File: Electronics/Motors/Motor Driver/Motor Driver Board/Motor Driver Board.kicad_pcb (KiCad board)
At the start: 2 copper layers, 136 parts, among them IC1 STM32H723ZGT6, IC2 TJA1057GT/3, IC3 ESDA6V1W5, IC4 ESDA6V1W5, IC5 TPS54295PWPR, J1 TYPE-C-31-M-12, J2 Screw_Terminal_01x02, J3 TC2030, J4 XT60PW-F, J5 XT60PW-F, J6 XT60PW-F, J7 XT60PW-M, J8 Screw_Terminal_01x02, SW1 SW_DIP_x02, T1 NVMFS4C05NT1G, T10 NVMFS4C05NT1G, T11 NVMFS4C05NT1G, T12 NVMFS4C05NT1G, T2 NVMFS4C05NT1G, T3 NVMFS4C05NT1G, T4 NVMFS4C05NT1G, T5 NVMFS4C05NT1G, T6 NVMFS4C05NT1G, T7 NVMFS4C05NT1G, T8 NVMFS4C05NT1G, T9 NVMFS4C05NT1G, U1 LSM6DS3, U2 DRV8701ERGER, U3 DRV8701ERGER, U4 DRV8701ERGER, X1 25MHz_Clock, X2 32.768kHz_Clock

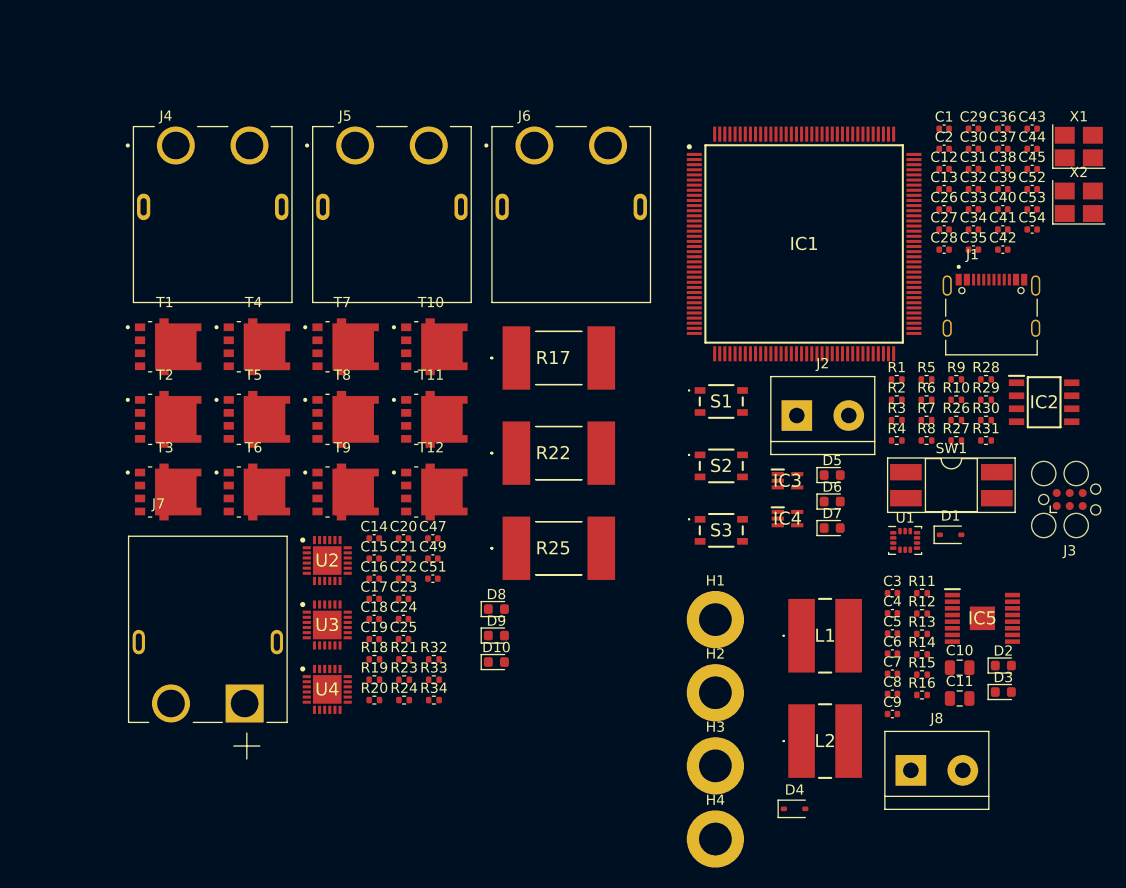
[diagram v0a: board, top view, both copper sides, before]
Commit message: Schematic updates
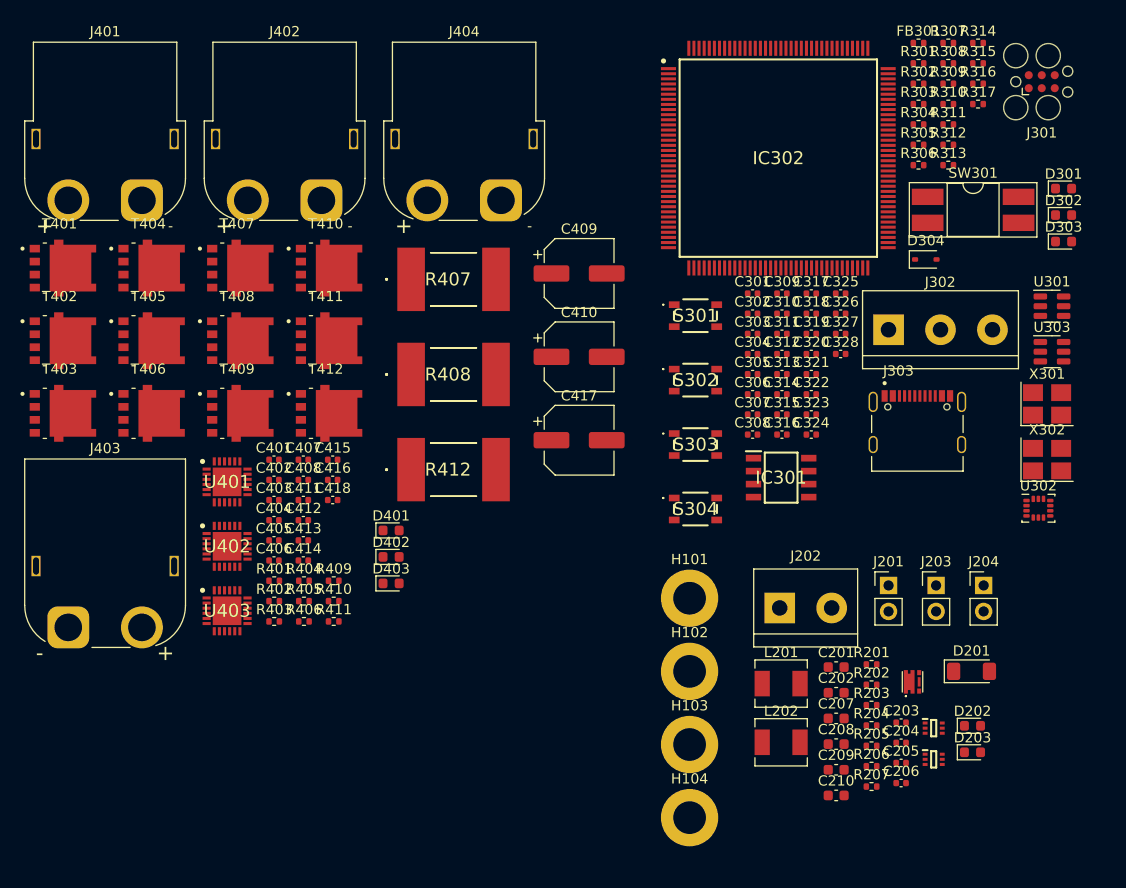
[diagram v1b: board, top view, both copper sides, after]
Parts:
- removed C1, C12, C13, C15, C2, C20, C24, C28, C30, C32, C33, C34, C35, C36, C37, C39, C40, C41, C42, C43, C44, C47, C49, C51, C7, C8: 100n, Capacitor_SMD:C_0402_1005Metric
- removed C10, C11: 47u, Capacitor_SMD:C_0805_2012Metric
- removed C14, C16, C17, C18, C19, C21, C22, C23, C25, C29, C31, C9: 1u, Capacitor_SMD:C_0402_1005Metric
- removed C26, C27: 2u2, Capacitor_SMD:C_0402_1005Metric
- removed C3, C38, C4, C45: 10u, Capacitor_SMD:C_0402_1005Metric
- removed C5, C52, C53, C54, C6: 10n, Capacitor_SMD:C_0402_1005Metric
- removed D1, D4: BAT760-115, Diode_SMD:D_SOD-323
- removed D10, D5, D8, D9: Red, LED_SMD:LED_0603_1608Metric
- removed D2, D3: LED_R, LED_SMD:LED_0603_1608Metric
- removed D6: Green, LED_SMD:LED_0603_1608Metric
- removed D7: Blue, LED_SMD:LED_0603_1608Metric
- removed H1, H2, H3, H4: MountingHole_Pad, MountingHole:MountingHole_3.2mm_M3_DIN965_Pad
- removed IC1: STM32H723ZGT6, MSL Footprints:QFP50P2200X2200X160-144N
- removed IC2: TJA1057GT/3, MSL Footprints:SOIC127P600X175-8N
- removed IC3, IC4: ESDA6V1W5, footprints:SOT65P210X110-5N
- removed IC5: TPS54295PWPR, MSL Footprints:SOP65P640X120-17N
- removed J1: TYPE-C-31-M-12, MSL Footprints:HRO_TYPE-C-31-M-12
- removed J2, J8: Screw_Terminal_01x02, TerminalBlock:TerminalBlock_bornier-2_P5.08mm
- removed J3: TC2030, Connector:Tag-Connect_TC2030-IDC-FP_2x03_P1.27mm_Vertical
- removed J4, J5, J6: XT60PW-F, MSL Footprints:AMASS_XT60PW-F
- removed J7: XT60PW-M, MSL Footprints:AMASS_XT60PW-M
- removed L1: 3u3, MSL Footprints:29332C
- removed L2: 2u2, MSL Footprints:29222C
- removed R1, R15, R2, R3, R4, R5, R6: 2k2, Resistor_SMD:R_0402_1005Metric
- removed R10, R14, R18, R19, R20, R21, R23, R24, R26, R27, R28: 10k, Resistor_SMD:R_0402_1005Metric
- removed R11: 124k, Resistor_SMD:R_0402_1005Metric
- removed R12: 22k1, Resistor_SMD:R_0402_1005Metric
- removed R13: 33k, Resistor_SMD:R_0402_1005Metric
- removed R16, R29, R30, R31, R32, R33, R34: 1k5, Resistor_SMD:R_0402_1005Metric
- removed R17, R22, R25: CSS2H-3920K-5L00F, MSL Footprints:CSS2H3920K5L00F
- removed R7, R8: 5k1, Resistor_SMD:R_0402_1005Metric
- removed R9: 120R, Resistor_SMD:R_0402_1005Metric
- removed S1, S2, S3: TS20-42-25-WT-160-SMT-TR, MSL Footprints:TS204225WT160SMTTRMSL
- removed SW1: SW_DIP_x02, Package_DIP:DIP-4_W8.89mm_SMDSocket_LongPads
- removed T1, T10, T11, T12, T2, T3, T4, T5, T6, T7, T8, T9: NVMFS4C05NT1G, MSL Footprints:TRANS_NVMFS5834NLWFT1G
- removed U1: LSM6DS3, Package_LGA:LGA-14_3x2.5mm_P0.5mm_LayoutBorder3x4y
- removed U2, U3, U4: DRV8701ERGER, MSL Footprints:QFN50P400X400X100-25N-D
- removed X1: 25MHz_Clock, Oscillator:Oscillator_SMD_Abracon_ASE-4Pin_3.2x2.5mm_HandSoldering
- removed X2: 32.768kHz_Clock, Oscillator:Oscillator_SMD_Abracon_ASE-4Pin_3.2x2.5mm_HandSoldering
- added C201: 22u, Capacitor_SMD:C_0603_1608Metric, F.Cu at (172.6, 109.8)
- added C202: 22u, Capacitor_SMD:C_0603_1608Metric, F.Cu at (172.6, 112.3)
- added C203: 100n, Capacitor_SMD:C_0402_1005Metric, F.Cu at (178.9, 115.2)
- added C204: 100n, Capacitor_SMD:C_0402_1005Metric, F.Cu at (178.9, 117.2)
- added C205: 100n, Capacitor_SMD:C_0402_1005Metric, F.Cu at (178.9, 119.2)
- added C206: 100n, Capacitor_SMD:C_0402_1005Metric, F.Cu at (178.9, 121.1)
- added C207: 22u, Capacitor_SMD:C_0603_1608Metric, F.Cu at (172.6, 114.8)
- added C208: 22u, Capacitor_SMD:C_0603_1608Metric, F.Cu at (172.6, 117.3)
- added C209: 22u, Capacitor_SMD:C_0603_1608Metric, F.Cu at (172.6, 119.8)
- added C210: 22u, Capacitor_SMD:C_0603_1608Metric, F.Cu at (172.6, 122.3)
- added C301: 100n, Capacitor_SMD:C_0402_1005Metric, F.Cu at (164.4, 73.3)
- added C302: 100n, Capacitor_SMD:C_0402_1005Metric, F.Cu at (164.4, 75.2)
- added C303: 10n, Capacitor_SMD:C_0402_1005Metric, F.Cu at (164.4, 77.2)
- added C304: 10n, Capacitor_SMD:C_0402_1005Metric, F.Cu at (164.4, 79.2)
- added C305: 10n, Capacitor_SMD:C_0402_1005Metric, F.Cu at (164.4, 81.1)
- added C306: 100n, Capacitor_SMD:C_0402_1005Metric, F.Cu at (164.4, 83.1)
- added C307: 1u, Capacitor_SMD:C_0402_1005Metric, F.Cu at (164.4, 85.1)
- added C308: 100n, Capacitor_SMD:C_0402_1005Metric, F.Cu at (164.4, 87.0)
- added C309: 100n, Capacitor_SMD:C_0402_1005Metric, F.Cu at (167.3, 73.3)
- added C310: 100n, Capacitor_SMD:C_0402_1005Metric, F.Cu at (167.3, 75.2)
- added C311: 1u, Capacitor_SMD:C_0402_1005Metric, F.Cu at (167.3, 77.2)
- added C312: 100n, Capacitor_SMD:C_0402_1005Metric, F.Cu at (167.3, 79.2)
- added C313: 100n, Capacitor_SMD:C_0402_1005Metric, F.Cu at (167.3, 81.1)
- added C314: 100n, Capacitor_SMD:C_0402_1005Metric, F.Cu at (167.3, 83.1)
- added C315: 100n, Capacitor_SMD:C_0402_1005Metric, F.Cu at (167.3, 85.1)
- added C316: 10u, Capacitor_SMD:C_0402_1005Metric, F.Cu at (167.3, 87.0)
- added C317: 100n, Capacitor_SMD:C_0402_1005Metric, F.Cu at (170.1, 73.3)
- added C318: 100n, Capacitor_SMD:C_0402_1005Metric, F.Cu at (170.1, 75.2)
- added C319: 100n, Capacitor_SMD:C_0402_1005Metric, F.Cu at (170.1, 77.2)
- added C320: 100n, Capacitor_SMD:C_0402_1005Metric, F.Cu at (170.1, 79.2)
- added C321: 2u2, Capacitor_SMD:C_0402_1005Metric, F.Cu at (170.1, 81.1)
- added C322: 100n, Capacitor_SMD:C_0402_1005Metric, F.Cu at (170.1, 83.1)
- added C323: 100n, Capacitor_SMD:C_0402_1005Metric, F.Cu at (170.1, 85.1)
- added C324: 10u, Capacitor_SMD:C_0402_1005Metric, F.Cu at (170.1, 87.0)
- added C325: 2u2, Capacitor_SMD:C_0402_1005Metric, F.Cu at (173.0, 73.3)
- added C326: 100n, Capacitor_SMD:C_0402_1005Metric, F.Cu at (173.0, 75.2)
- added C327: 100n, Capacitor_SMD:C_0402_1005Metric, F.Cu at (173.0, 77.2)
- added C328: 10n, Capacitor_SMD:C_0402_1005Metric, F.Cu at (173.0, 79.2)
- added C401: 1u, Capacitor_SMD:C_0402_1005Metric, F.Cu at (117.6, 89.5)
- added C402: 1u, Capacitor_SMD:C_0402_1005Metric, F.Cu at (117.6, 91.5)
- added C403: 1u, Capacitor_SMD:C_0402_1005Metric, F.Cu at (117.6, 93.5)
- added C404: 1u, Capacitor_SMD:C_0402_1005Metric, F.Cu at (117.6, 95.4)
- added C405: 100n, Capacitor_SMD:C_0402_1005Metric, F.Cu at (117.6, 97.4)
- added C406: 100n, Capacitor_SMD:C_0402_1005Metric, F.Cu at (117.6, 99.4)
- added C407: 1u, Capacitor_SMD:C_0402_1005Metric, F.Cu at (120.5, 89.5)
- added C408: 1u, Capacitor_SMD:C_0402_1005Metric, F.Cu at (120.5, 91.5)
- added C409: 100u, Capacitor_SMD:CP_Elec_6.3x7.7, F.Cu at (147.4, 71.3)
- added C410: 100u, Capacitor_SMD:CP_Elec_6.3x7.7, F.Cu at (147.4, 79.5)
- added C411: 100n, Capacitor_SMD:C_0402_1005Metric, F.Cu at (120.5, 93.5)
- added C412: 100n, Capacitor_SMD:C_0402_1005Metric, F.Cu at (120.5, 95.4)
- added C413: 1u, Capacitor_SMD:C_0402_1005Metric, F.Cu at (120.5, 97.4)
- added C414: 1u, Capacitor_SMD:C_0402_1005Metric, F.Cu at (120.5, 99.4)
- added C415: 100n, Capacitor_SMD:C_0402_1005Metric, F.Cu at (123.3, 89.5)
- added C416: 1u, Capacitor_SMD:C_0402_1005Metric, F.Cu at (123.3, 91.5)
- added C417: 100u, Capacitor_SMD:CP_Elec_6.3x7.7, F.Cu at (147.4, 87.6)
- added C418: 100n, Capacitor_SMD:C_0402_1005Metric, F.Cu at (123.3, 93.5)
- added D201: ZMM10V, Diode_SMD:D_MiniMELF, F.Cu at (185.8, 110.2)
- added D202: GREEN, LED_SMD:LED_0603_1608Metric, F.Cu at (185.9, 115.5)
- added D203: GREEN, LED_SMD:LED_0603_1608Metric, F.Cu at (185.9, 118.1)
- added D301: Red, LED_SMD:LED_0603_1608Metric, F.Cu at (194.8, 63.0)
- added D302: Green, LED_SMD:LED_0603_1608Metric, F.Cu at (194.8, 65.6)
- added D303: Blue, LED_SMD:LED_0603_1608Metric, F.Cu at (194.8, 68.2)
- added D304: BAT760-115, Diode_SMD:D_SOD-323, F.Cu at (181.3, 69.9)
- added D401: Red, LED_SMD:LED_0603_1608Metric, F.Cu at (129.1, 96.4)
- added D402: Red, LED_SMD:LED_0603_1608Metric, F.Cu at (129.1, 99.0)
- added D403: Red, LED_SMD:LED_0603_1608Metric, F.Cu at (129.1, 101.6)
- added FB301: 120R@100MHz, Resistor_SMD:R_0402_1005Metric, F.Cu at (180.6, 48.8)
- added H101: MountingHole_Pad, MountingHole:MountingHole_3.2mm_M3_DIN965_Pad, F.Cu at (158.2, 103.0)
- added H102: MountingHole_Pad, MountingHole:MountingHole_3.2mm_M3_DIN965_Pad, F.Cu at (158.2, 110.2)
- added H103: MountingHole_Pad, MountingHole:MountingHole_3.2mm_M3_DIN965_Pad, F.Cu at (158.2, 117.3)
- added H104: MountingHole_Pad, MountingHole:MountingHole_3.2mm_M3_DIN965_Pad, F.Cu at (158.2, 124.5)
- added IC201: TPS563202DRLR, MSL Footprints:SOTFL50P160X60-6N, F.Cu at (182.1, 115.8)
- added IC202: TPS563202DRLR, MSL Footprints:SOTFL50P160X60-6N, F.Cu at (182.1, 118.8)
- added IC301: TJA1057GT/3, MSL Footprints:SOIC127P600X175-8N, F.Cu at (167.2, 91.3)
- added IC302: STM32H723ZGT6, MSL Footprints:QFP50P2200X2200X160-144N, F.Cu at (166.9, 60.0)
- added J201: Conn_01x02_Pin, Connector_PinHeader_2.54mm:PinHeader_1x02_P2.54mm_Vertical, F.Cu at (177.7, 101.8)
- added J202: Screw_Terminal_01x02, TerminalBlock:TerminalBlock_bornier-2_P5.08mm, F.Cu at (167.0, 104.0)
- added J203: Conn_01x02_Pin, Connector_PinHeader_2.54mm:PinHeader_1x02_P2.54mm_Vertical, F.Cu at (182.3, 101.8)
- added J204: Conn_01x02_Pin, Connector_PinHeader_2.54mm:PinHeader_1x02_P2.54mm_Vertical, F.Cu at (187.0, 101.8)
- added J301: TC2030, Connector:Tag-Connect_TC2030-IDC-FP_2x03_P1.27mm_Vertical, F.Cu at (192.7, 52.5)
- added J302: Screw_Terminal_01x03, TerminalBlock:TerminalBlock_bornier-3_P5.08mm, F.Cu at (177.7, 76.8)
- added J303: TYPE-C-31-M-12, MSL Footprints:HRO_TYPE-C-31-M-12, F.Cu at (180.5, 88.0)
- added J401: XT60PW-F, Connector_AMASS:AMASS_XT60PW-F_1x02_P7.20mm_Horizontal, F.Cu at (104.7, 64.2)
- added J402: XT60PW-F, Connector_AMASS:AMASS_XT60PW-F_1x02_P7.20mm_Horizontal, F.Cu at (122.2, 64.2)
- added J403: XT60PW-M, Connector_AMASS:AMASS_XT60PW-M_1x02_P7.20mm_Horizontal, F.Cu at (97.5, 105.9)
- added J404: XT60PW-F, Connector_AMASS:AMASS_XT60PW-F_1x02_P7.20mm_Horizontal, F.Cu at (139.8, 64.2)
- added L201: 4u7, Inductor_SMD:L_Chilisin_BMRA00040420, F.Cu at (167.2, 111.4)
- added L202: 3u3, Inductor_SMD:L_Chilisin_BMRA00040420, F.Cu at (167.2, 117.1)
- added Q201: DMP3028LFDE, MSL Footprints:DMP2066UFDE7, F.Cu at (180.0, 111.2)
- added R201: 330R, Resistor_SMD:R_0402_1005Metric, F.Cu at (176.0, 109.5)
- added R202: 52k, Resistor_SMD:R_0402_1005Metric, F.Cu at (176.0, 111.5)
- added R203: 10k, Resistor_SMD:R_0402_1005Metric, F.Cu at (176.0, 113.5)
- added R204: 31k, Resistor_SMD:R_0402_1005Metric, F.Cu at (176.0, 115.5)
- added R205: 10k, Resistor_SMD:R_0402_1005Metric, F.Cu at (176.0, 117.5)
- added R206: 2k2, Resistor_SMD:R_0402_1005Metric, F.Cu at (176.0, 119.5)
- added R207: 1k5, Resistor_SMD:R_0402_1005Metric, F.Cu at (176.0, 121.5)
- added R301: 1k5, Resistor_SMD:R_0402_1005Metric, F.Cu at (180.6, 50.8)
- added R302: 1k5, Resistor_SMD:R_0402_1005Metric, F.Cu at (180.6, 52.8)
- added R303: 1k5, Resistor_SMD:R_0402_1005Metric, F.Cu at (180.6, 54.7)
- added R304: 10k, Resistor_SMD:R_0402_1005Metric, F.Cu at (180.6, 56.7)
- added R305: 10k, Resistor_SMD:R_0402_1005Metric, F.Cu at (180.6, 58.7)
- added R306: 10k, Resistor_SMD:R_0402_1005Metric, F.Cu at (180.6, 60.7)
- added R307: 120R, Resistor_SMD:R_0402_1005Metric, F.Cu at (183.5, 48.8)
- added R308: 10k, Resistor_SMD:R_0402_1005Metric, F.Cu at (183.5, 50.8)
- added R309: 5k1, Resistor_SMD:R_0402_1005Metric, F.Cu at (183.5, 52.8)
- added R310: 5k1, Resistor_SMD:R_0402_1005Metric, F.Cu at (183.5, 54.7)
- added R311: 2k2, Resistor_SMD:R_0402_1005Metric, F.Cu at (183.5, 56.7)
- added R312: 2k2, Resistor_SMD:R_0402_1005Metric, F.Cu at (183.5, 58.7)
- added R313: 2k2, Resistor_SMD:R_0402_1005Metric, F.Cu at (183.5, 60.7)
- added R314: 2k2, Resistor_SMD:R_0402_1005Metric, F.Cu at (186.4, 48.8)
- added R315: 2k2, Resistor_SMD:R_0402_1005Metric, F.Cu at (186.4, 50.8)
- added R316: 2k2, Resistor_SMD:R_0402_1005Metric, F.Cu at (186.4, 52.8)
- added R317: 10k, Resistor_SMD:R_0402_1005Metric, F.Cu at (186.4, 54.7)
- added R401: 1k5, Resistor_SMD:R_0402_1005Metric, F.Cu at (117.6, 101.3)
- added R402: 1k5, Resistor_SMD:R_0402_1005Metric, F.Cu at (117.6, 103.3)
- added R403: 10k, Resistor_SMD:R_0402_1005Metric, F.Cu at (117.6, 105.3)
- added R404: 10k, Resistor_SMD:R_0402_1005Metric, F.Cu at (120.5, 101.3)
- added R405: 10k, Resistor_SMD:R_0402_1005Metric, F.Cu at (120.5, 103.3)
- added R406: 10k, Resistor_SMD:R_0402_1005Metric, F.Cu at (120.5, 105.3)
- added R407: CSS2H-3920K-5L00F, MSL Footprints:CSS2H3920K5L00F, F.Cu at (135.2, 71.9)
- added R408: CSS2H-3920K-5L00F, MSL Footprints:CSS2H3920K5L00F, F.Cu at (135.2, 81.2)
- added R409: 1k5, Resistor_SMD:R_0402_1005Metric, F.Cu at (123.4, 101.3)
- added R410: 10k, Resistor_SMD:R_0402_1005Metric, F.Cu at (123.4, 103.3)
- added R411: 10k, Resistor_SMD:R_0402_1005Metric, F.Cu at (123.4, 105.3)
- added R412: CSS2H-3920K-5L00F, MSL Footprints:CSS2H3920K5L00F, F.Cu at (135.2, 90.5)
- added S301: TS20-42-25-WT-160-SMT-TR, MSL Footprints:TS204225WT160SMTTRMSL, F.Cu at (158.8, 75.4)
- added S302: TS20-42-25-WT-160-SMT-TR, MSL Footprints:TS204225WT160SMTTRMSL, F.Cu at (158.8, 81.7)
- added S303: TS20-42-25-WT-160-SMT-TR, MSL Footprints:TS204225WT160SMTTRMSL, F.Cu at (158.8, 88.0)
- added S304: TS20-42-25-WT-160-SMT-TR, MSL Footprints:TS204225WT160SMTTRMSL, F.Cu at (158.8, 94.3)
- added SW301: SW_DIP_x02, Package_DIP:DIP-4_W8.89mm_SMDSocket_LongPads, F.Cu at (186.0, 65.1)
- added T401: NVMFS4C05NT1G, MSL Footprints:TRANS_NVMFS5834NLWFT1G, F.Cu at (97.0, 70.8)
- added T402: NVMFS4C05NT1G, MSL Footprints:TRANS_NVMFS5834NLWFT1G, F.Cu at (97.0, 77.9)
- added T403: NVMFS4C05NT1G, MSL Footprints:TRANS_NVMFS5834NLWFT1G, F.Cu at (97.0, 85.0)
- added T404: NVMFS4C05NT1G, MSL Footprints:TRANS_NVMFS5834NLWFT1G, F.Cu at (105.6, 70.8)
- added T405: NVMFS4C05NT1G, MSL Footprints:TRANS_NVMFS5834NLWFT1G, F.Cu at (105.6, 77.9)
- added T406: NVMFS4C05NT1G, MSL Footprints:TRANS_NVMFS5834NLWFT1G, F.Cu at (105.6, 85.0)
- added T407: NVMFS4C05NT1G, MSL Footprints:TRANS_NVMFS5834NLWFT1G, F.Cu at (114.3, 70.8)
- added T408: NVMFS4C05NT1G, MSL Footprints:TRANS_NVMFS5834NLWFT1G, F.Cu at (114.3, 77.9)
- added T409: NVMFS4C05NT1G, MSL Footprints:TRANS_NVMFS5834NLWFT1G, F.Cu at (114.3, 85.0)
- added T410: NVMFS4C05NT1G, MSL Footprints:TRANS_NVMFS5834NLWFT1G, F.Cu at (123.0, 70.8)
- added T411: NVMFS4C05NT1G, MSL Footprints:TRANS_NVMFS5834NLWFT1G, F.Cu at (123.0, 77.9)
- added T412: NVMFS4C05NT1G, MSL Footprints:TRANS_NVMFS5834NLWFT1G, F.Cu at (123.0, 85.0)
- added U301: USBLC6-4SC6-ES, Package_TO_SOT_SMD:SOT-23-6, F.Cu at (193.7, 74.5)
- added U302: LSM6DS3, Package_LGA:LGA-14_3x2.5mm_P0.5mm_LayoutBorder3x4y, F.Cu at (192.3, 94.2)
- added U303: USBLC6-4SC6-ES, Package_TO_SOT_SMD:SOT-23-6, F.Cu at (193.7, 79.0)
- added U401: DRV8701ERGER, MSL Footprints:QFN50P400X400X100-25N-D, F.Cu at (113.0, 91.7)
- added U402: DRV8701ERGER, MSL Footprints:QFN50P400X400X100-25N-D, F.Cu at (113.0, 98.0)
- added U403: DRV8701ERGER, MSL Footprints:QFN50P400X400X100-25N-D, F.Cu at (113.0, 104.3)
- added X301: 25MHz_Clock, Oscillator:Oscillator_SMD_Abracon_ASE-4Pin_3.2x2.5mm_HandSoldering, F.Cu at (193.2, 84.0)
- added X302: 32.768kHz_Clock, Oscillator:Oscillator_SMD_Abracon_ASE-4Pin_3.2x2.5mm_HandSoldering, F.Cu at (193.2, 89.5)

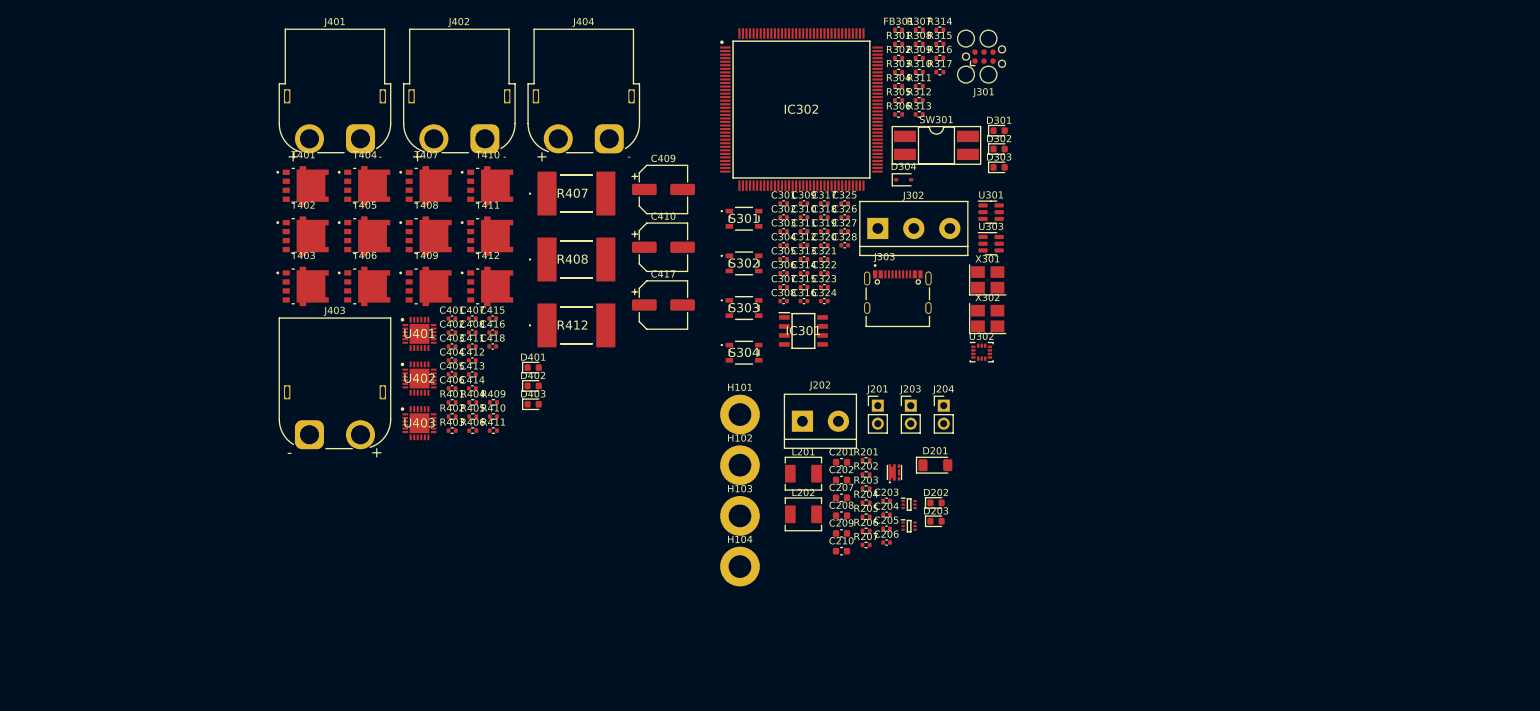
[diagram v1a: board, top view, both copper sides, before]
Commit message: PCB layout progress, spice simulations for power board
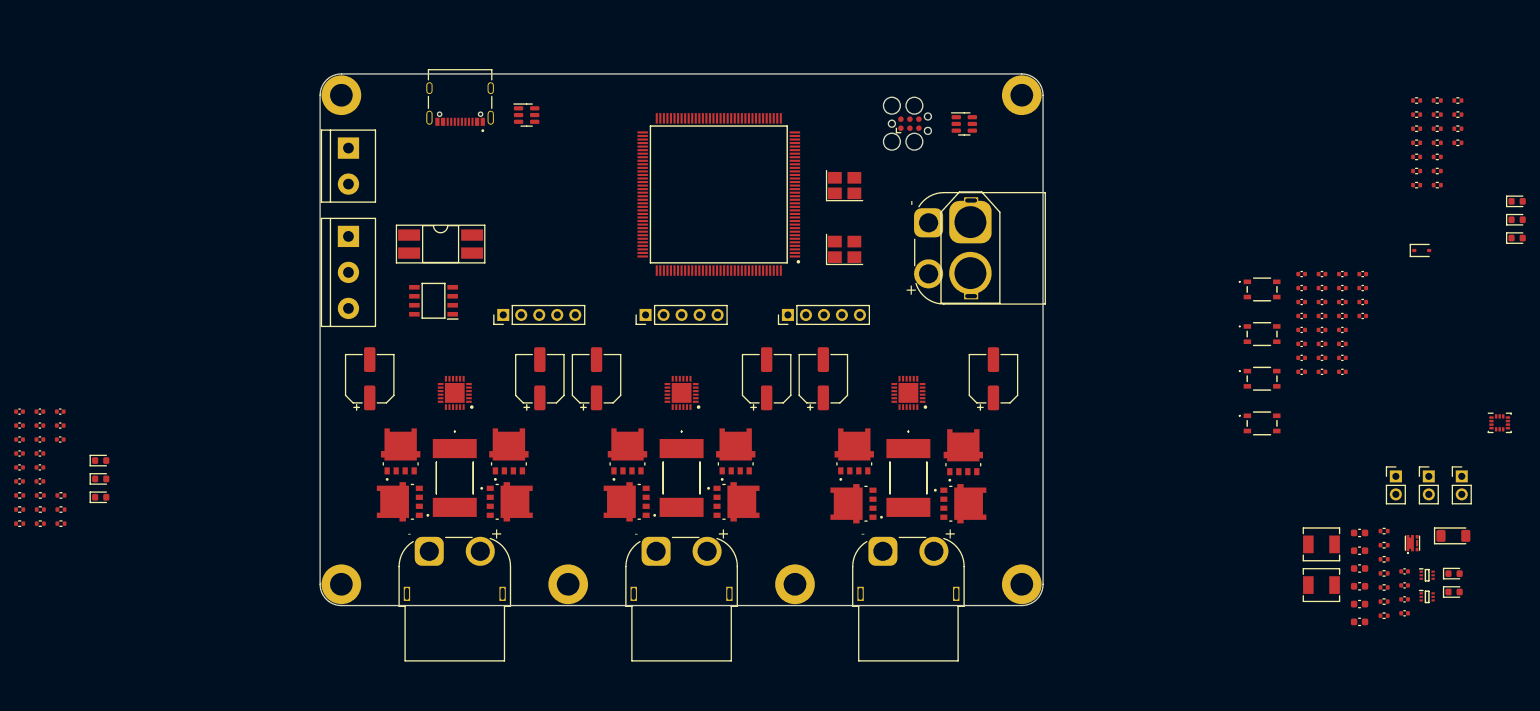
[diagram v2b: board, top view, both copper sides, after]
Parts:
- added C419: 100u, Capacitor_SMD:CP_Elec_6.3x7.7, F.Cu at (170.0, 98.0)
- added C420: 100u, Capacitor_SMD:CP_Elec_6.3x7.7, F.Cu at (106.0, 98.0)
- added C421: 100u, Capacitor_SMD:CP_Elec_6.3x7.7, F.Cu at (138.0, 98.0)
- added H105: MountingHole_Pad, MountingHole:MountingHole_3.2mm_M3_DIN965_Pad, F.Cu at (134.0, 127.0)
- added H106: MountingHole_Pad, MountingHole:MountingHole_3.2mm_M3_DIN965_Pad, F.Cu at (166.0, 127.0)
- added J405: XT60-M-Vertical, MSL Footprints:AMASS_XT60-M_1x02_P7.20mm_Vertical, F.Cu at (190.8, 75.9)
- added J406: Conn_01x05, Connector_PinHeader_2.54mm:PinHeader_1x05_P2.54mm_Vertical, F.Cu at (124.8, 89.0)
- added J407: Conn_01x05, Connector_PinHeader_2.54mm:PinHeader_1x05_P2.54mm_Vertical, F.Cu at (144.9, 89.0)
- added J408: Conn_01x05, Connector_PinHeader_2.54mm:PinHeader_1x05_P2.54mm_Vertical, F.Cu at (165.0, 89.0)
- J401, J402, J404: footprint Connector_AMASS:AMASS_XT60PW-F_1x02_P7.20mm_Horizontal -> MSL Footprints:AMASS_XT60PW-F_1x02_P7.20mm_Horizontal
- J403: footprint Connector_AMASS:AMASS_XT60PW-M_1x02_P7.20mm_Horizontal -> MSL Footprints:AMASS_XT60PW-M_1x02_P7.20mm_Horizontal
- moved T402 100.2 mm to (189.7, 115.6)
- moved T401 100.1 mm to (189.7, 108.4), turned to 90 degrees
- moved J401 93.9 mm to (178.4, 122.3), turned to 180 degrees
- moved J403 92.3 mm to (184.8, 76.0), turned to -90 degrees
- moved T403 83.1 mm to (174.3, 115.6), turned to 180 degrees
- moved T404 78.3 mm to (174.4, 108.3), turned to 90 degrees
- moved J202 74.7 mm to (103.0, 65.5), turned to -90 degrees
- moved J302 74.7 mm to (103.0, 77.9), turned to -90 degrees
- moved C201 73.8 mm to (245.7, 119.8)
- moved C202 73.8 mm to (245.7, 122.3)
- moved C203 73.8 mm to (252.0, 125.2)
- moved C204 73.8 mm to (252.0, 127.2)
- moved C205 73.8 mm to (252.0, 129.1)
- moved C206 73.8 mm to (252.0, 131.1)
- moved C207 73.8 mm to (245.7, 124.8)
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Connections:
- J302 pad 1: /Microcontroller/CANH -> /Microcontroller/CANL
- J302 pad 3: /Microcontroller/CANL -> /Microcontroller/CANH
- J403 pad 1: VMOT -> GND
- J403 pad 2: GND -> VMOT
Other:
- board outline added: 102 x 75 mm

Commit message: Finished power board layout
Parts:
- removed U301: USBLC6-4SC6-ES, Package_TO_SOT_SMD:SOT-23-6
- moved J202 95.8 mm to (196.2, 87.5), turned to 90 degrees
- moved J302 93.3 mm to (196.2, 75.1), turned to 90 degrees
- moved J405 81.4 mm to (109.5, 80.8), turned to 90 degrees
- moved IC301 71.7 mm to (184.8, 70.5), turned to 0 degrees
- moved J403 69.6 mm to (115.4, 80.8), turned to 90 degrees
- moved SW301 64.3 mm to (180.2, 81.8), turned to 180 degrees
- moved J303 61.5 mm to (180.2, 57.0)
- moved U303 52.3 mm to (180.2, 65.0), turned to 90 degrees
- moved X302 46.1 mm to (128.5, 67.8)
- moved X301 44.6 mm to (128.5, 73.0)
- moved J301 14.5 mm to (167.8, 60.5)
- moved IC302 7.95 mm to (147.5, 70.2), turned to 0 degrees
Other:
- copper layers 2 -> 4
